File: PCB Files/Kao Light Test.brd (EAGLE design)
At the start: 68.6 x 53.3 mm, 23 parts, among them T1 2N2222

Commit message: feat: Grounds the Cable's housing.
Also updates the images in the ReadMe
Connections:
- net GND_1: now also DIGITAL-OUT.G1, DIGITAL-OUT.G2
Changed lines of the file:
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@@
 <vertex x="-7.62" y="53.34"/>
 </polygon>
+<contactref element="DIGITAL-OUT" pad="G2"/>
+<contactref element="DIGITAL-OUT" pad="G1"/>
 </signal>
 <signal name="VIN">

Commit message: docs: Updates the PCB and ReadMe to be clearer
The PCB was updated so that the servos are labeled as what they are
instead of as numbers. One resistor was also updated and all other
digital grounds were connected to the ground plane.
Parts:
- R14: value 220 -> 1k
- renumbered SERVO1 to PAN_SERVO, SERVO2 to TILT_SERVO
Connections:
- net GND_1: now also DIGITAL-OUT.1, DIGITAL-OUT.18, DIGITAL-OUT.2, DIGITAL-OUT.23, DIGITAL-OUT.3, DIGITAL-OUT.8
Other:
- board text added: "Laser State"
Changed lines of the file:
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@@
 <fusionsync huburn="a.YnVzaW5lc3M6Z21haWwxOTMxNzE5" projecturn="a.YnVzaW5lc3M6Z21haWwxOTMxNzE5I0QyMDIxMDgyNzQzNzk4ODk4MQ" f3durn="urn:adsk.wipprod:dm.lineage:TNS2zfh-TQqjS4NN-gPOGQ" pcbguid="15db3e48-d778-4921-8b97-5cc11880282f" lastpulledtime="" lastsyncedchangeguid="ca1e5789-fbb9-cde9-2695-c8db211853fd" latestrevisionid="" lastsyncedrevisionid="" lastboardhashguid="9e2937fb-2267-ce90-ea09-409f92429b17" lastpushedtime="2021-09-09T14:31:41Z" linktopcb3d="false"/>
 <plain>
-<text x="57.15" y="10.16" size="1.778" layer="25" rot="R90">Battery</text>
+<text x="55.88" y="8.89" size="1.778" layer="25" rot="R180">Battery</text>
 <text x="54.61" y="40.64" size="1.778" layer="25" rot="R90">Laser</text>
 <text x="10.16" y="45.72" size="1.778" layer="25" align="center">Kao Light Test
 V3</text>
+<text x="58.42" y="6.35" size="1.778" layer="25" rot="R90">Laser State</text>
 </plain>
 <attributes>
@@
 <attribute name="VALUE" x="62.865" y="44.831" size="0.6096" layer="27" font="vector" ratio="20" rot="R270"/>
 </element>
-<element name="SERVO2" library="adafruit" library_urn="urn:adsk.eagle:library:420" package="1X03-CLEANBIG" package3d_urn="urn:adsk.eagle:package:6240706/1" override_package3d_urn="urn:adsk.eagle:package:30732786/2" override_package_urn="urn:adsk.eagle:footprint:6240060/1" value="" x="27.94" y="44.45" smashed="yes">
-<attribute name="NAME" x="24.0538" y="46.2788" size="1.27" layer="25" ratio="10"/>
+<element name="TILT_SERVO" library="adafruit" library_urn="urn:adsk.eagle:library:420" package="1X03-CLEANBIG" package3d_urn="urn:adsk.eagle:package:6240706/1" override_package3d_urn="urn:adsk.eagle:package:30732786/2" override_package_urn="urn:adsk.eagle:footprint:6240060/1" value="" x="27.94" y="44.45" smashed="yes">
+<attribute name="NAME" x="21.5138" y="46.2788" size="1.27" layer="25" ratio="10"/>
 <attribute name="VALUE" x="24.13" y="41.275" size="1.27" layer="27"/>
 </element>
-<element name="SERVO1" library="adafruit" library_urn="urn:adsk.eagle:library:420" package="1X03-CLEANBIG" package3d_urn="urn:adsk.eagle:package:6240706/1" override_package3d_urn="urn:adsk.eagle:package:30732786/2" override_package_urn="urn:adsk.eagle:footprint:6240060/1" value="" x="38.1" y="44.45" smashed="yes">
+<element name="PAN_SERVO" library="adafruit" library_urn="urn:adsk.eagle:library:420" package="1X03-CLEANBIG" package3d_urn="urn:adsk.eagle:package:6240706/1" override_package3d_urn="urn:adsk.eagle:package:30732786/2" override_package_urn="urn:adsk.eagle:footprint:6240060/1" value="" x="38.1" y="44.45" smashed="yes">
 <attribute name="NAME" x="34.2138" y="46.2788" size="1.27" layer="25" ratio="10"/>
 <attribute name="VALUE" x="34.29" y="41.275" size="1.27" layer="27"/>
@@
 <attribute name="VALUE" x="53.086" y="37.846" size="0.6096" layer="27" font="vector" ratio="20" align="top-center"/>
 </element>
-<element name="R14" library="SparkFun-Resistors" library_urn="urn:adsk.eagle:library:532" package="AXIAL-0.3" package3d_urn="urn:adsk.eagle:package:39658/1" value="220" x="46.482" y="45.085" smashed="yes">
+<element name="R14" library="SparkFun-Resistors" library_urn="urn:adsk.eagle:library:532" package="AXIAL-0.3" package3d_urn="urn:adsk.eagle:package:39658/1" value="1k" x="46.482" y="45.085" smashed="yes">
 <attribute name="NAME" x="46.482" y="46.101" size="0.6096" layer="25" font="vector" ratio="20" align="bottom-center"/>
 <attribute name="PROD_ID" value="RES-8371" x="46.482" y="45.085" size="1.778" layer="27" display="off"/>
@@
 </signal>
 <signal name="TILT">
-<contactref element="SERVO2" pad="3"/>
+<contactref element="TILT_SERVO" pad="3"/>
 <contactref element="U$1" pad="D11"/>
 <wire x1="34.036" y1="50.8" x2="30.48" y2="47.244" width="0.4064" layer="1"/>
@@
 <signal name="PAN">
 <contactref element="U$1" pad="D10"/>
-<contactref element="SERVO1" pad="3"/>
+<contactref element="PAN_SERVO" pad="3"/>
 <wire x1="40.64" y1="44.45" x2="40.64" y2="46.99" width="0.4064" layer="1"/>
 <wire x1="40.64" y1="46.99" x2="36.83" y2="50.8" width="0.4064" layer="1"/>
@@
 <contactref element="PULL_DOWN_RESISTORS:R2" pad="P$1"/>
 <contactref element="CN1" pad="2"/>
-<contactref element="SERVO2" pad="1"/>
-<contactref element="SERVO1" pad="1"/>
+<contactref element="TILT_SERVO" pad="1"/>
+<contactref element="PAN_SERVO" pad="1"/>
 <contactref element="5V_REG" pad="4"/>
 <wire x1="38.1" y1="39.37" x2="34.417" y2="39.37" width="0.4064" layer="1"/>
@@
 <contactref element="DIGITAL-OUT" pad="G2"/>
 <contactref element="DIGITAL-OUT" pad="G1"/>
+<contactref element="DIGITAL-OUT" pad="23"/>
+<contactref element="DIGITAL-OUT" pad="8"/>
+<contactref element="DIGITAL-OUT" pad="18"/>
+<contactref element="DIGITAL-OUT" pad="3"/>
+<contactref element="DIGITAL-OUT" pad="2"/>
+<contactref element="DIGITAL-OUT" pad="1"/>
 </signal>
 <signal name="VIN">
@@
 </signal>
 <signal name="5VOUT">
-<contactref element="SERVO2" pad="2"/>
-<contactref element="SERVO1" pad="2"/>
+<contactref element="TILT_SERVO" pad="2"/>
+<contactref element="PAN_SERVO" pad="2"/>
 <contactref element="5V_REG" pad="3"/>
 <contactref element="LASER" pad="2"/>

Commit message: docs: Updates PCB and ReadMe based on testing
Updates the PCB resistor values and images of the PCB based on the
testing done in the previous commit.
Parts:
- PULL_DOWN_RESISTORS:R1, PULL_DOWN_RESISTORS:R10, PULL_DOWN_RESISTORS:R11, PULL_DOWN_RESISTORS:R12, PULL_DOWN_RESISTORS:R2, PULL_DOWN_RESISTORS:R3, PULL_DOWN_RESISTORS:R4, PULL_DOWN_RESISTORS:R5, PULL_DOWN_RESISTORS:R6, PULL_DOWN_RESISTORS:R7, PULL_DOWN_RESISTORS:R8, PULL_DOWN_RESISTORS:R9: value 1k -> 10k
- R14: value 1k -> 220

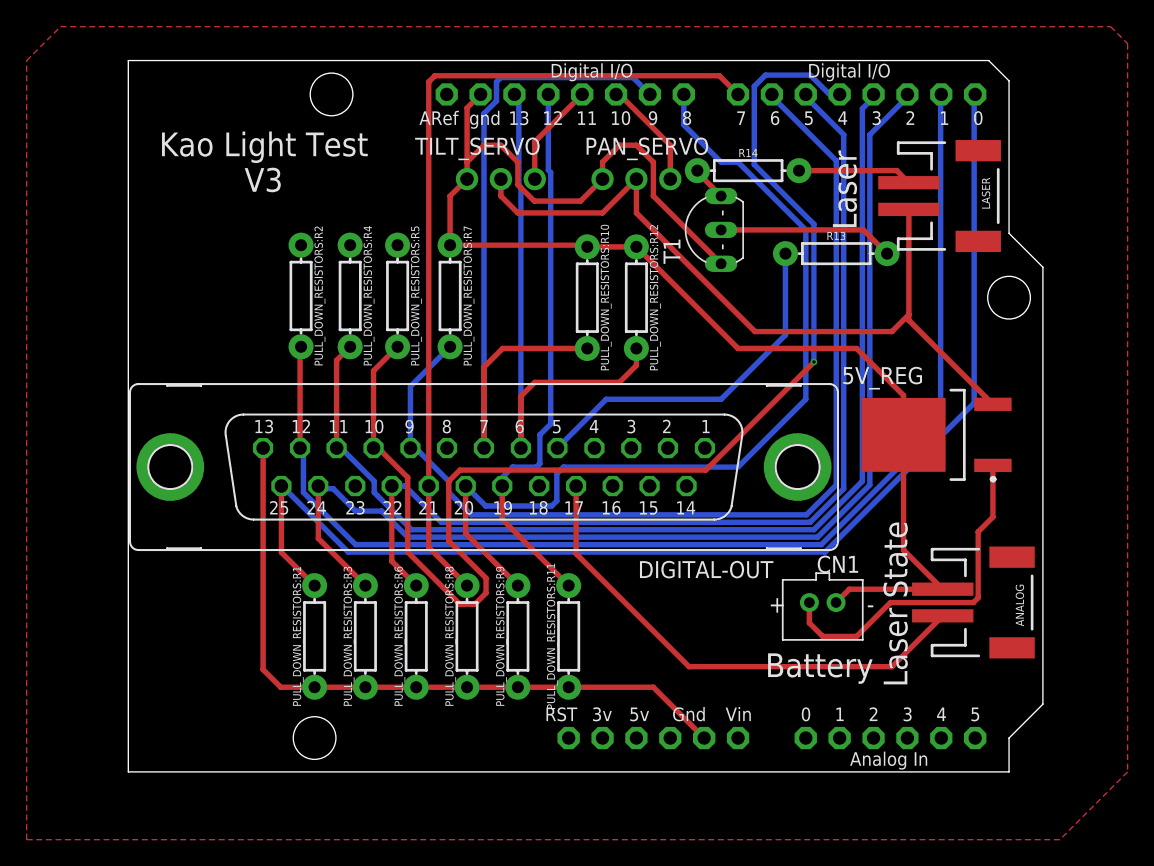
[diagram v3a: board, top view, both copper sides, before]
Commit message: feat: Adds two more digital outputs to tilt angles
Updates the GUI, Arduino code, and PCB for two more digital outputs to
up the tilt angles from 32 to 128 angles. Also addresses small fixes.

Closes #18 issue
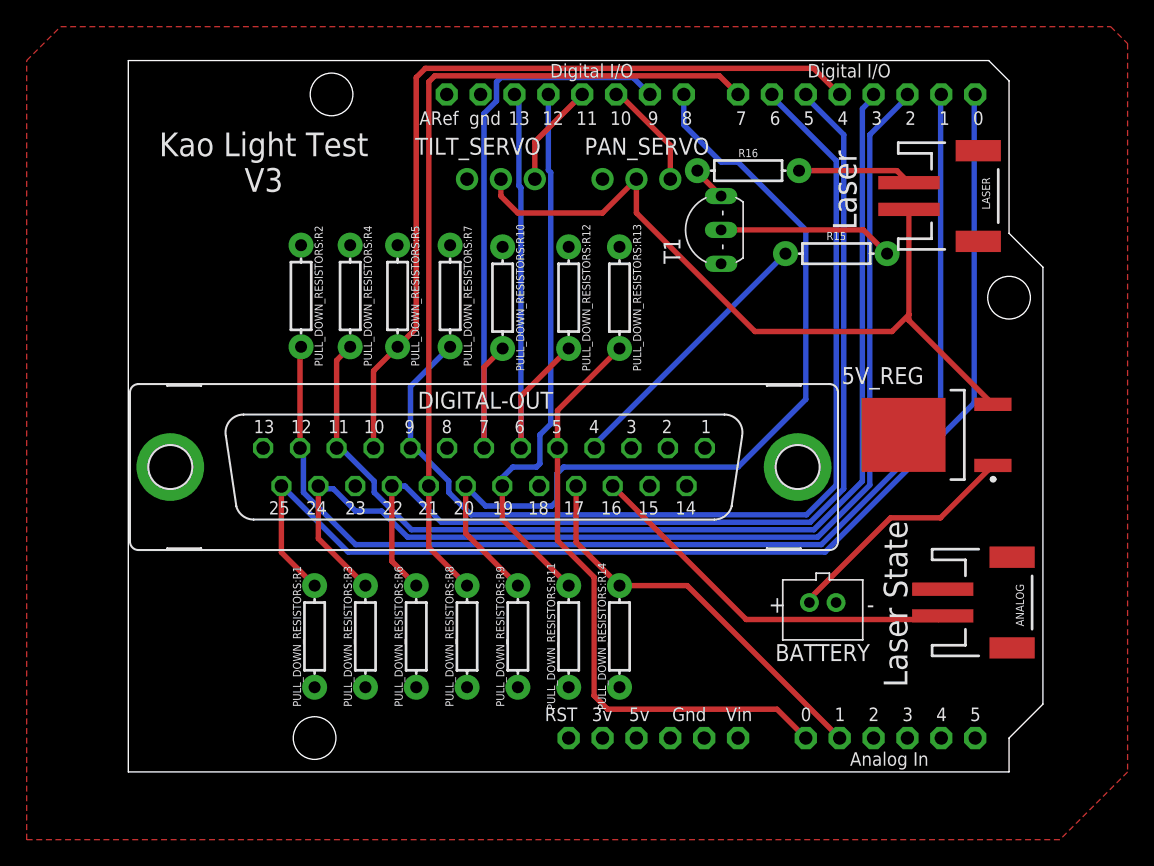
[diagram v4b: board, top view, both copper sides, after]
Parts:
- added PULL_DOWN_RESISTORS:R13, PULL_DOWN_RESISTORS:R14: 10k, SparkFun-Resistors:AXIAL-0.3
- moved PULL_DOWN_RESISTORS:R10 6.35 mm to (28.1, 35.6)
- moved PULL_DOWN_RESISTORS:R12 5.08 mm to (33.0, 35.6)
- renumbered CN1 to BATTERY, R13 to R15, R14 to R16
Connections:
- new net D15: DIGITAL-OUT.4, R15.P$1
- new net D16: ANALOG.2, DIGITAL-OUT.16
- net D13: now also PULL_DOWN_RESISTORS:R13.P$2, U$1.A0; no longer R15.P$1
- net D14: now also PULL_DOWN_RESISTORS:R14.P$2, U$1.A1; no longer ANALOG.2
- net GND_1: now also PULL_DOWN_RESISTORS:R13.P$1, PULL_DOWN_RESISTORS:R14.P$1
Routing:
- net GND_1: track 156.8 -> 0.00 mm
- net D5: track 96.5 -> 62.0 mm, vias 1 -> 0
- net D16: track 0.00 -> 29.0 mm
- net D15: track 0.00 -> 20.5 mm
- net D13: track 26.7 -> 46.3 mm
- net BAT+: track 26.2 -> 18.2 mm
- net D14: track 37.7 -> 30.1 mm
- net D10: track 54.4 -> 48.1 mm
- net D12: track 41.5 -> 35.7 mm
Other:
- board text removed: "Battery"
